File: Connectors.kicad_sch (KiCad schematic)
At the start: 4 parts, among them J1 Conn_01x09_Pin, J2 Conn_01x04_Pin, J3 Conn_01x04_Pin, J4 Conn_02x03_Odd_Even

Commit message: Completed comments.
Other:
- moved on the sheet: J3
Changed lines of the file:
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@@
 	(hierarchical_label "RX"
 		(shape input)
-		(at 161.29 95.25 0)
+		(at 166.37 95.25 0)
 		(effects
 			(font
@@
 	(hierarchical_label "GND"
 		(shape passive)
-		(at 161.29 90.17 0)
+		(at 166.37 90.17 0)
 		(effects
 			(font
@@
 	(hierarchical_label "TX"
 		(shape output)
-		(at 161.29 97.79 0)
+		(at 166.37 97.79 0)
 		(effects
 			(font
@@
 	(hierarchical_label "Vcc"
 		(shape passive)
-		(at 161.29 92.71 0)
+		(at 166.37 92.71 0)
 		(effects
 			(font
@@
 			)
 			(justify left)
+		)
+	)
+	(rule_area
+		(polyline
+			(pts
+				(xy 119.38 76.2) (xy 184.15 76.2) (xy 184.15 146.05) (xy 119.38 146.05)
+			)
+			(stroke
+				(width 0)
+				(type dash)
+				(color 0 0 255 1)
+			)
+			(fill
+				(type none)
+			)
 		)
 	)
@@
 	(symbol
 		(lib_id "EG:Conn_01x04_Pin")
-		(at 156.21 92.71 0)
+		(at 161.29 92.71 0)
 		(unit 1)
 		(exclude_from_sim no)
@@
 		(dnp no)
 		(property "Reference" "J3"
-			(at 156.845 85.09 0)
+			(at 161.925 85.09 0)
 			(effects
 				(font
@@
 		)
 		(property "Value" "Conn_01x04_Pin"
-			(at 156.845 87.63 0)
+			(at 161.925 87.63 0)
 			(effects
 				(font
@@
 		)
 		(property "Footprint" ""
-			(at 156.21 92.71 0)
+			(at 161.29 92.71 0)
 			(effects
 				(font
@@
 		)
 		(property "Datasheet" "~"
-			(at 156.21 92.71 0)
+			(at 161.29 92.71 0)
 			(effects
 				(font
@@
 		)
 		(property "Description" "Generic connector, single row, 01x04, script generated"
-			(at 156.21 92.71 0)
+			(at 161.29 92.71 0)
 			(effects
 				(font
@@
 		)
 		(property "Purpose" "Serial UART"
-			(at 158.242 99.822 0)
-			(effects
-				(font
+			(at 163.322 99.822 0)
+			(effects
+				(font

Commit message: Completed footprints assignments.
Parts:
- J1: footprint (none) -> Connector_PinHeader_2.54mm:PinHeader_1x09_P2.54mm_Vertical
- J2, J3: footprint (none) -> Connector_PinHeader_2.54mm:PinHeader_1x04_P2.54mm_Vertical
- J4: footprint (none) -> Connector_PinHeader_2.54mm:PinHeader_2x03_P2.54mm_Vertical
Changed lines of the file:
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@@
 			)
 		)
-		(property "Footprint" ""
+		(property "Footprint" "Connector_PinHeader_2.54mm:PinHeader_2x03_P2.54mm_Vertical"
 			(at 165.1 127 0)
 			(effects
@@
 			)
 		)
-		(property "Footprint" ""
+		(property "Footprint" "Connector_PinHeader_2.54mm:PinHeader_1x04_P2.54mm_Vertical"
 			(at 134.62 92.71 0)
 			(effects
@@
 			)
 		)
-		(property "Footprint" ""
+		(property "Footprint" "Connector_PinHeader_2.54mm:PinHeader_1x04_P2.54mm_Vertical"
 			(at 161.29 92.71 0)
 			(effects
@@
 			)
 		)
-		(property "Footprint" ""
+		(property "Footprint" "Connector_PinHeader_2.54mm:PinHeader_1x09_P2.54mm_Vertical"
 			(at 134.62 124.46 0)
 			(effects

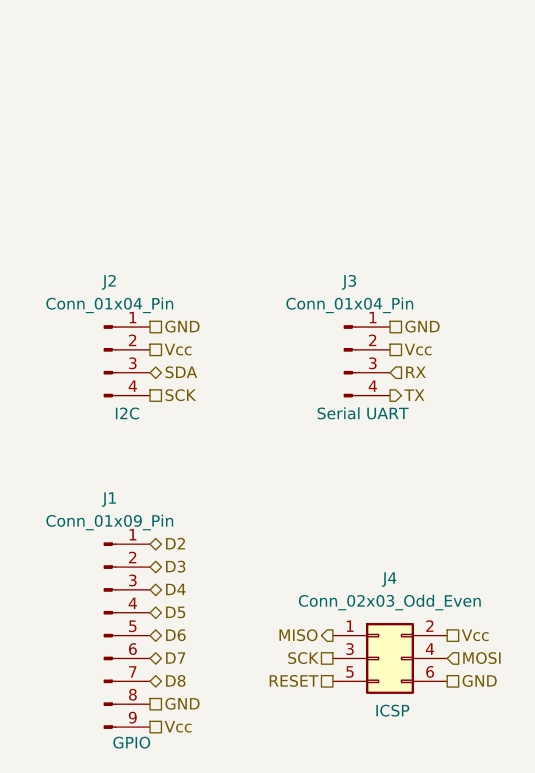
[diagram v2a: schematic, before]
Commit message: Fixed two defects in the schematic.
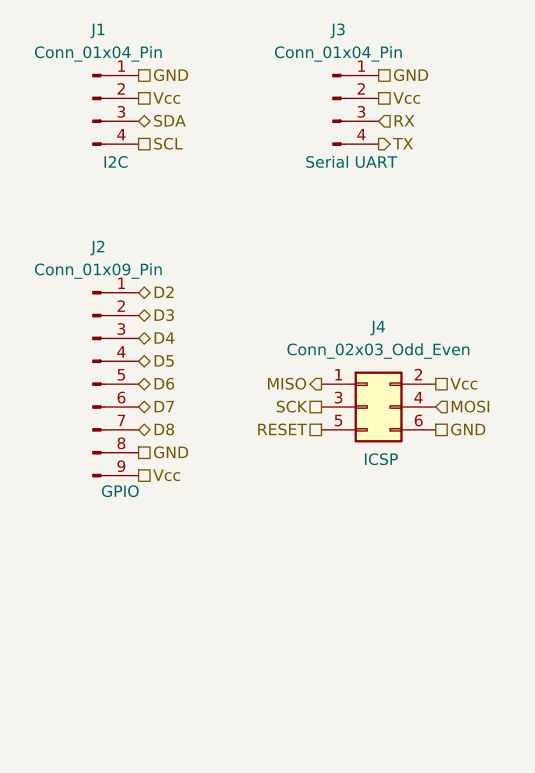
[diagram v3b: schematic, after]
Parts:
- renumbered J2 to J1, J1 to J2
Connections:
- net SCK: no longer J1.4 (Pin_4)
- new net SCL: J1.4 (Pin_4)
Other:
- moved on the sheet: J1, J2, J3, J4
